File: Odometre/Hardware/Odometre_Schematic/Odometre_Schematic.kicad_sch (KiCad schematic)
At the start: 26 parts, among them IC1 STM32C092FCP6, J1 Conn_01x03_Pin, J2 Conn_01x03_Pin, J3 Conn_Alim, J4 Conn_Laser1, J5 Conn_Laser2, J6 Conn_02x05_Odd_Even, SW1 SW_Push, SW2 SW_SPST, U1 MCP2562-E-SN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

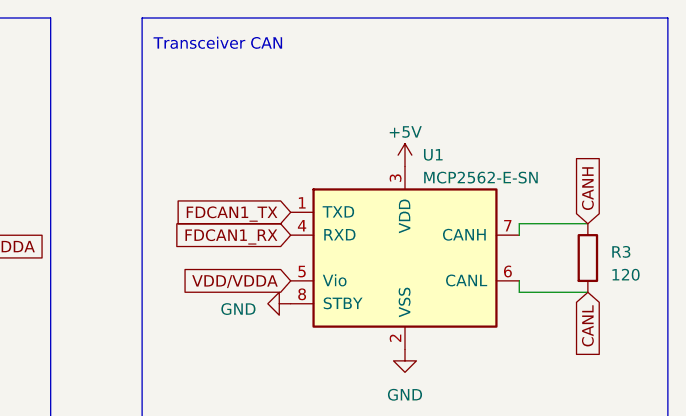
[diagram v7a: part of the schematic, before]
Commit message: modif tension d'entrée
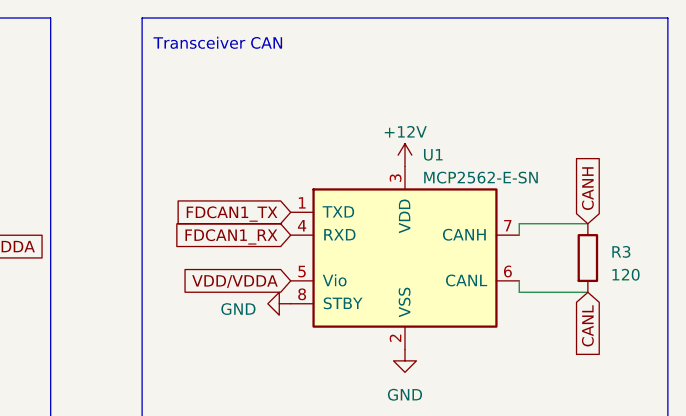
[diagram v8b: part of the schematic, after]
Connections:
- net +5V is gone; now on net +12V: U1.3 (VDD)
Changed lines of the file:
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@@
-    )
-  )
-  (symbol (lib_id "power:+5V") (at 242.57 39.37 0) (unit 1)
-    (in_bom yes) (on_board yes) (dnp no) (fields_autoplaced)
-    (property "Reference" "#PWR09" (at 242.57 43.18 0)
-      (effects (font (size 1.27 1.27)) hide)
-    )
-    (property "Value" "+5V" (at 242.57 35.56 0)
-      (effects (font (size 1.27 1.27)))
-    )
-    (property "Footprint" "" (at 242.57 39.37 0)
-      (effects (font (size 1.27 1.27)) hide)
-    )
-    (property "Datasheet" "" (at 242.57 39.37 0)
-      (effects (font (size 1.27 1.27)) hide)
-    )
-    (pin "1")
-    (instances
-      (project "Odometre_Schematic"
-        (path "/3741a7b9-879e-49a1-88bd-82d63456a983"
-          (reference "#PWR09") (unit 1)
-        )
-      )
     )
   )
@@
         )
       )
+    )
+  )
+  (symbol (lib_id "power:+12V") (at 242.57 39.37 0) (unit 1)
+    (in_bom yes) (on_board yes) (dnp no) (fields_autoplaced)
+    (property "Reference" "#PWR09" (at 242.57 43.18 0)
+      (effects (font (size 1.27 1.27)) hide)
+    )
+    (property "Value" "+12V" (at 242.57 35.56 0)
+      (effects (font (size 1.27 1.27)))
+    )
+    (property "Footprint" "" (at 242.57 39.37 0)
+      (effects (font (size 1.27 1.27)) hide)
+    )
+    (property "Datasheet" "" (at 242.57 39.37 0)
+      (effects (font (size 1.27 1.27)) hide)
+    )
+    (pin "1")
+    (instances
+      (project "Odometre_Schematic"
+        (path "/3741a7b9-879e-49a1-88bd-82d63456a983"
+          (reference "#PWR09") (unit 1)
+        )
+      )
